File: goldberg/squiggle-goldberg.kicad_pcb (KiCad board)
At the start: 2 copper layers, 116 x 115.3 mm, 42 parts, among them SW1 switch, SW10 switch, SW11 switch, SW12 switch, SW13 switch, SW14 switch, SW15-1 switch, SW15-2 switch, SW16 switch, SW17 switch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

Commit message: Modified the goldberg design files for myself
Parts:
- added G***: LOGO, footprints:mokou-cute, F.Cu at (77.5, 52.1)
- added G***: LOGO, footprints:mokou-drugs, F.Cu at (76.2, 49.5)

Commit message: Updated the Goldberg PCB with correct memes
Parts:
- G***: moved to B.Cu
- moved G*** 1.27 mm to (76.2, 48.3), turned to 180 degrees

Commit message: Initial efforts towards adding I2C and LEDs
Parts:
- removed the G*** at (76.2, 48.3)
- U2: value ProMicro -> promicro-squiggle
- moved U2 0.19 mm to (125.7, 39.4)
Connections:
- U1 pad 4: (no net) -> Net-(U1-Pad4)
- U2 pad 1: (no net) -> Net-(U2-Pad1)
- U2 pad 17: (no net) -> Net-(U2-Pad17)
- U2 pad 18: (no net) -> Net-(U2-Pad18)
- U2 pad 19: (no net) -> Net-(U2-Pad19)
- U2 pad 2: (no net) -> Net-(U2-Pad2)
- U2 pad 20: (no net) -> Net-(U2-Pad20)
- U2 pad 22: (no net) -> Net-(U2-Pad22)
- U2 pad 24: (no net) -> Net-(U2-Pad24)
- U2 pad 3: (no net) -> Net-(U2-Pad3)
- U2 pad 4: (no net) -> Net-(U2-Pad4)
- U2 pad 5: (no net) -> Net-(U2-Pad5)
- U2 pad 7: (no net) -> Net-(U2-Pad7)

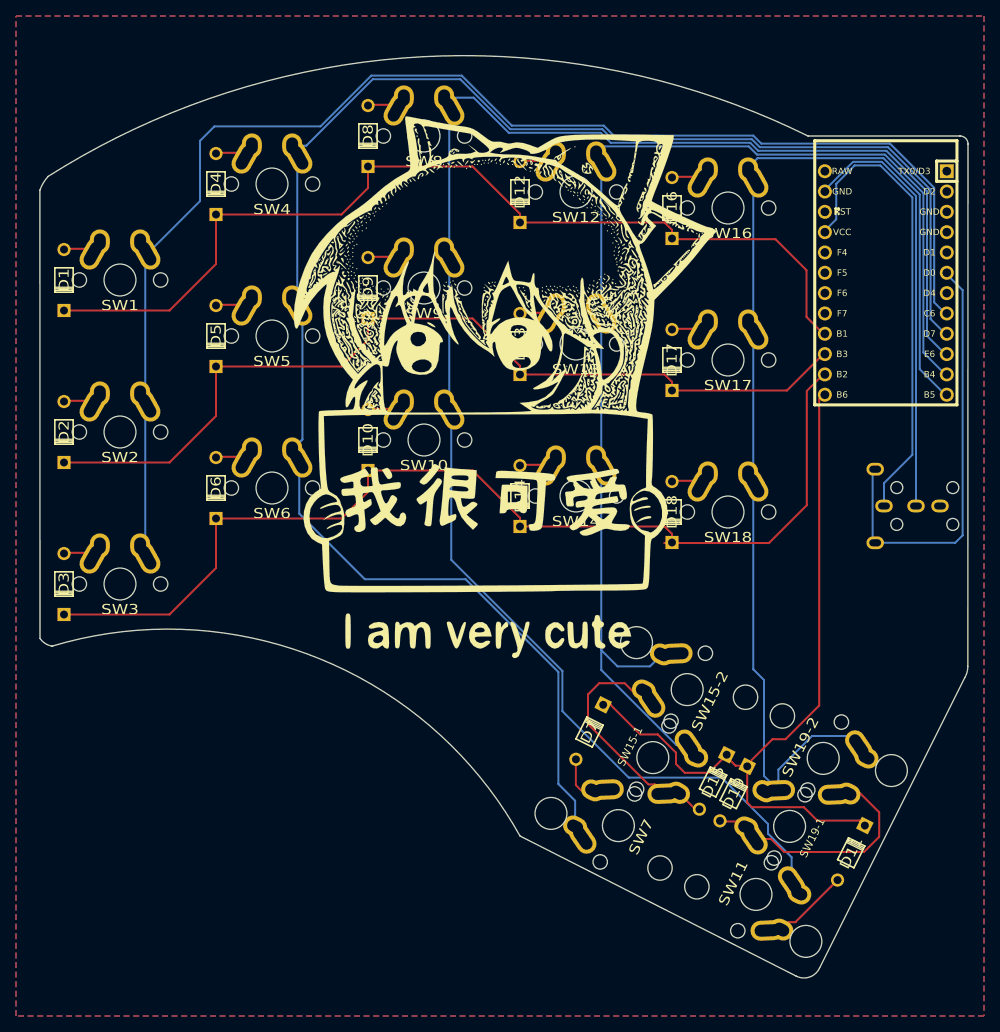
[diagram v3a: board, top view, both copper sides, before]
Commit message: Added OLED
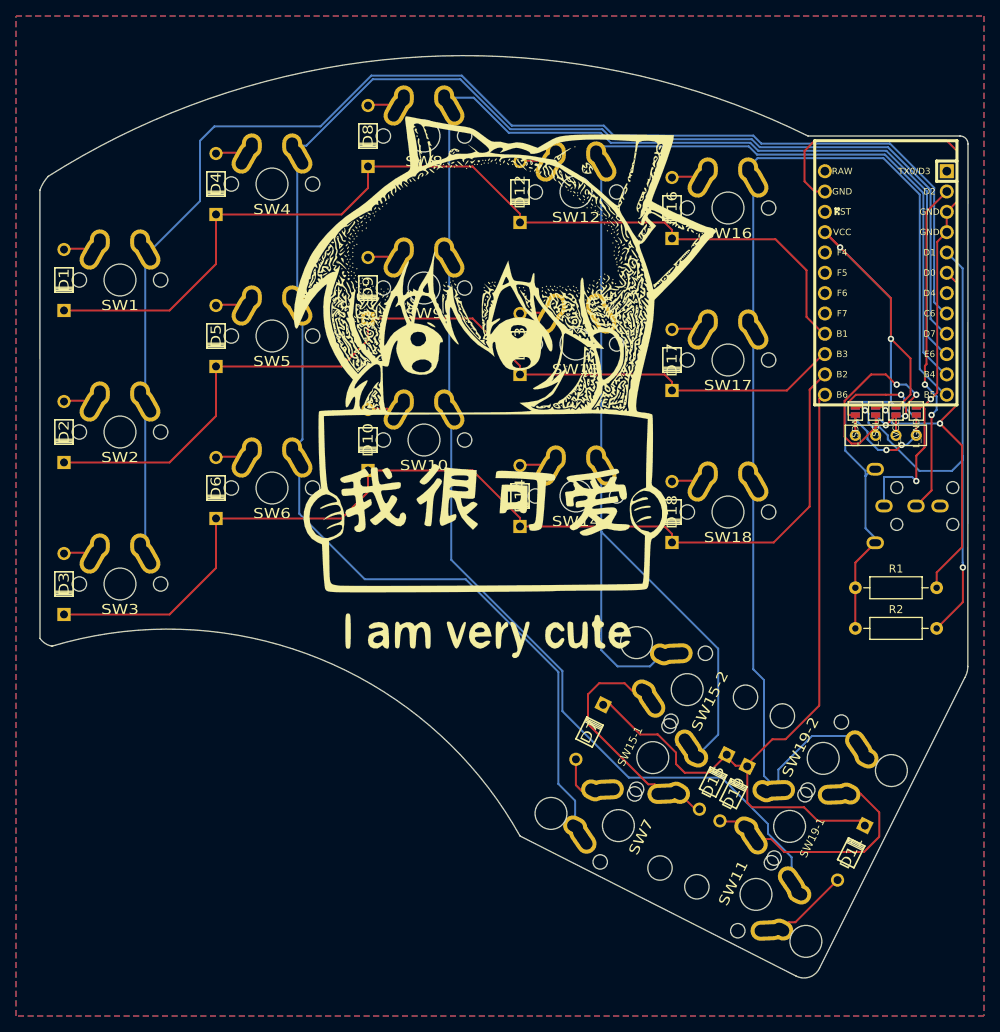
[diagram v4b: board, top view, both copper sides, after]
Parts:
- added JP1: L_GND, footprints:Jumper, F.Cu at (129.5, 55.4)
- added JP2: L_VCC, footprints:Jumper, F.Cu at (127.0, 55.4)
- added JP3: L_SCL, footprints:Jumper, F.Cu at (124.5, 55.4)
- added JP4: L_SDA, footprints:Jumper, F.Cu at (121.9, 55.4)
- added JP5: R_GND, footprints:Jumper, B.Cu at (129.5, 55.4)
- added JP6: R_VCC, footprints:Jumper, B.Cu at (127.0, 55.4)
- added JP7: R_SCL, footprints:Jumper, B.Cu at (124.5, 55.4)
- added JP8: R_SDA, footprints:Jumper, B.Cu at (121.9, 55.4)
- added P1: OLED, footprints:SSD_1306_128x32, B.Cu at (129.5, 58.4)
- added R1: 4.7K, Resistor_THT:R_Axial_DIN0207_L6.3mm_D2.5mm_P10.16mm_Horizontal, F.Cu at (121.9, 77.5)
- added R2: 4.7K, Resistor_THT:R_Axial_DIN0207_L6.3mm_D2.5mm_P10.16mm_Horizontal, F.Cu at (121.9, 82.5)
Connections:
- U1 pad 1: SDA -> VCC
- U1 pad 2: Net-(U1-Pad2) -> GND
- U1 pad 3: Net-(U1-Pad3) -> DATA
- U2 pad 2: Net-(U2-Pad2) -> DATA
- U2 pad 21: Net-(U1-Pad2) -> VCC
- U2 pad 23: Net-(U1-Pad3) -> GND
- U2 pad 3: Net-(U2-Pad3) -> GND
- U2 pad 4: Net-(U2-Pad4) -> GND
- U2 pad 5: Net-(U2-Pad5) -> SDA
- U2 pad 6: SDA -> SCL
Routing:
- net VCC: track 0.00 -> 99.5 mm, vias 0 -> 2
- net GND: track 0.00 -> 81.5 mm, vias 0 -> 2
- net Net-(U1-Pad2): track 58.9 -> 0.00 mm
- net SCL: track 0.00 -> 54.0 mm, vias 0 -> 2
- net Net-(U1-Pad3): track 53.6 -> 0.00 mm
- net DATA: track 0.00 -> 42.1 mm, vias 0 -> 2
- net Net-(JP3-Pad1): track 0.00 -> 29.6 mm, vias 0 -> 3
- net COL3: track 152.0 -> 171.2 mm
- net Net-(JP4-Pad1): track 0.00 -> 17.1 mm, vias 0 -> 1
- net SDA: track 54.5 -> 69.3 mm, vias 0 -> 2
- net Net-(JP1-Pad1): track 0.00 -> 13.6 mm, vias 0 -> 2
- net Net-(JP2-Pad1): track 0.00 -> 6.13 mm, vias 0 -> 1
- net ROW2: track 130.7 -> 130.0 mm
